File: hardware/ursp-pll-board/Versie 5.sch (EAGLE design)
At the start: 96 parts, among them IC1 MAX2870ETJ+T, IC2 LMK1C1103PWR, IC3 LMK1C1103PWR, IC4 LP5912-3.0DRVR, IC6 REF35180QDBVR, IC7 SN74AUP1T58DRYR, J1 60312202111527, J2 60312202111527, J3 60312202111527, J6 60312202111527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

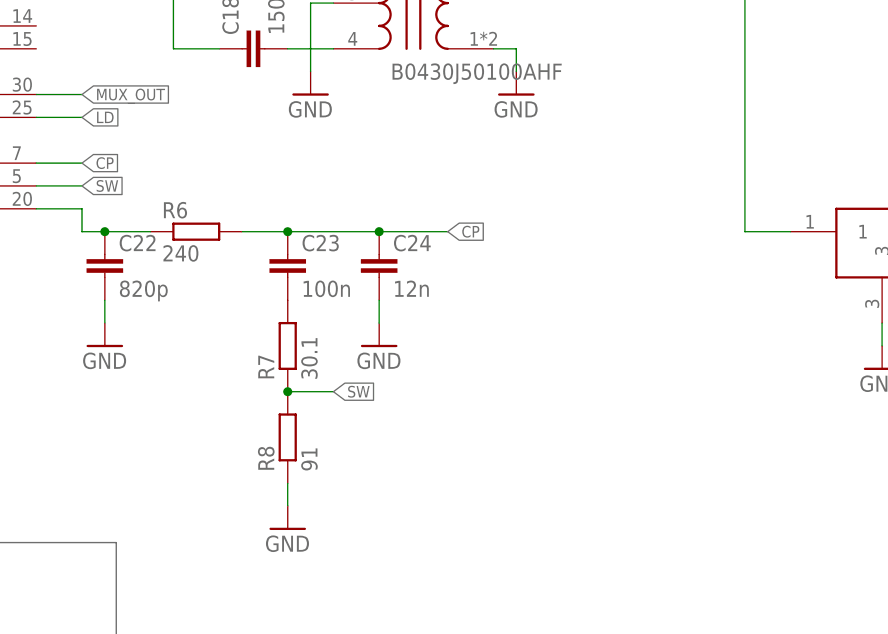
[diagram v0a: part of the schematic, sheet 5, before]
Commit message: Changed values of loop filter
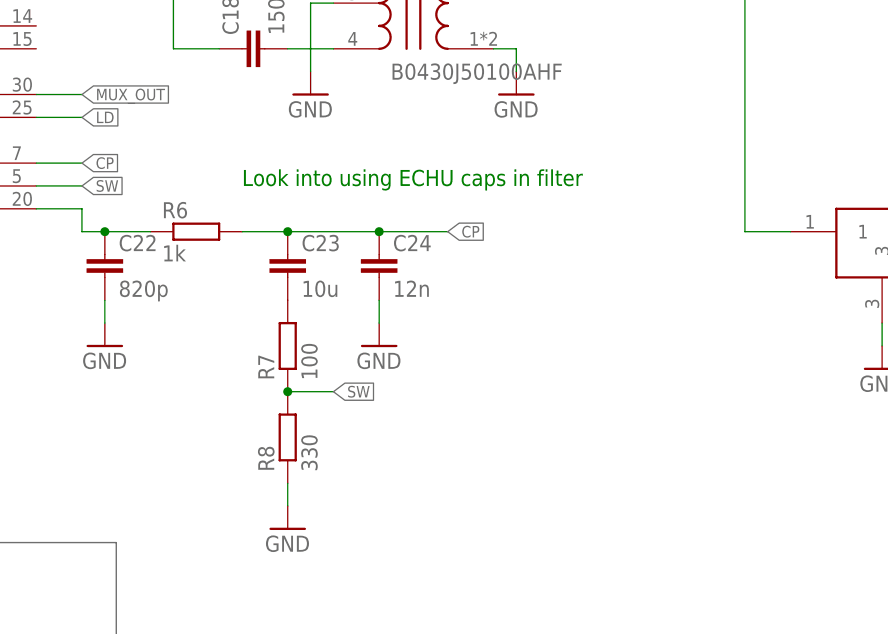
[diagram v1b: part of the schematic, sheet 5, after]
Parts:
- C23: value 100n -> 10u
- R6: value 240 -> 1k
- R7: value 30.1 -> 100
- R8: value 91 -> 330
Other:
- note added: "Look into using ECHU caps in filter"
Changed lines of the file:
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@@
 <part name="GND14" library="supply1" deviceset="GND" device=""/>
 <part name="C22" library="rcl" deviceset="C-EU" device="C0603" value="820p"/>
-<part name="R6" library="rcl" deviceset="R-EU_" device="R0603" value="240"/>
-<part name="C23" library="rcl" deviceset="C-EU" device="C0603" value="100n"/>
-<part name="R7" library="rcl" deviceset="R-EU_" device="R0603" value="30.1"/>
-<part name="R8" library="rcl" deviceset="R-EU_" device="R0603" value="91"/>
+<part name="R6" library="rcl" deviceset="R-EU_" device="R0603" value="1k"/>
+<part name="C23" library="rcl" deviceset="C-EU" device="C0603" value="10u"/>
+<part name="R7" library="rcl" deviceset="R-EU_" device="R0603" value="100"/>
+<part name="R8" library="rcl" deviceset="R-EU_" device="R0603" value="330"/>
 <part name="C24" library="rcl" deviceset="C-EU" device="C0603" value="12n"/>
 <part name="GND15" library="supply1" deviceset="GND" device=""/>
@@
 <wire x1="45.974" y1="46.736" x2="161.29" y2="46.736" width="0.1524" layer="95"/>
 <wire x1="161.29" y1="46.736" x2="161.29" y2="25.146" width="0.1524" layer="95"/>
+<text x="175.26" y="86.36" size="1.778" layer="91">Look into using ECHU caps in filter</text>
 </plain>
 <instances>
